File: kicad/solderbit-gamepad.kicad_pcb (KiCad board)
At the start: 2 copper layers, 114.5 x 45 mm, 28 parts, among them J1 Microbit, SW1 MST22D18G2 125, U1 74HC165

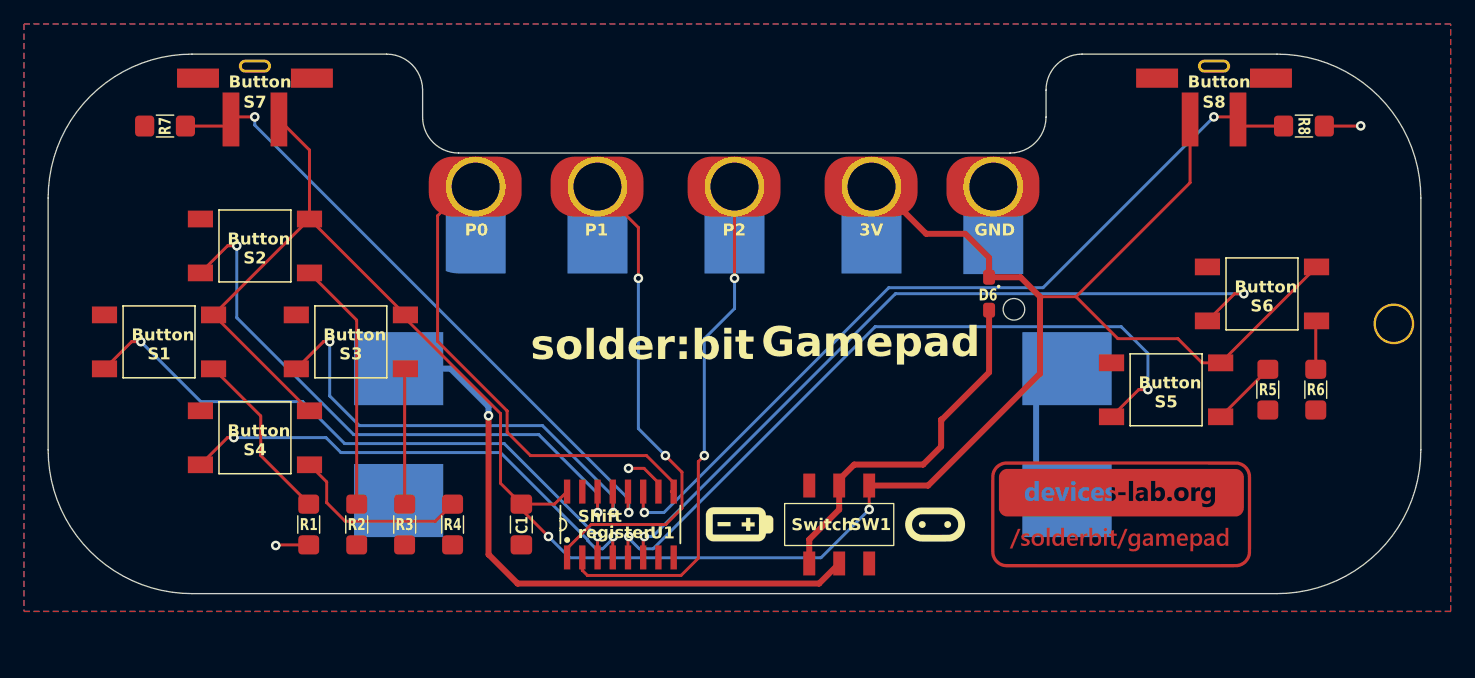
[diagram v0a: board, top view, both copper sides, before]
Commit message: Added all new project files and updated README.md for 2025 workshop
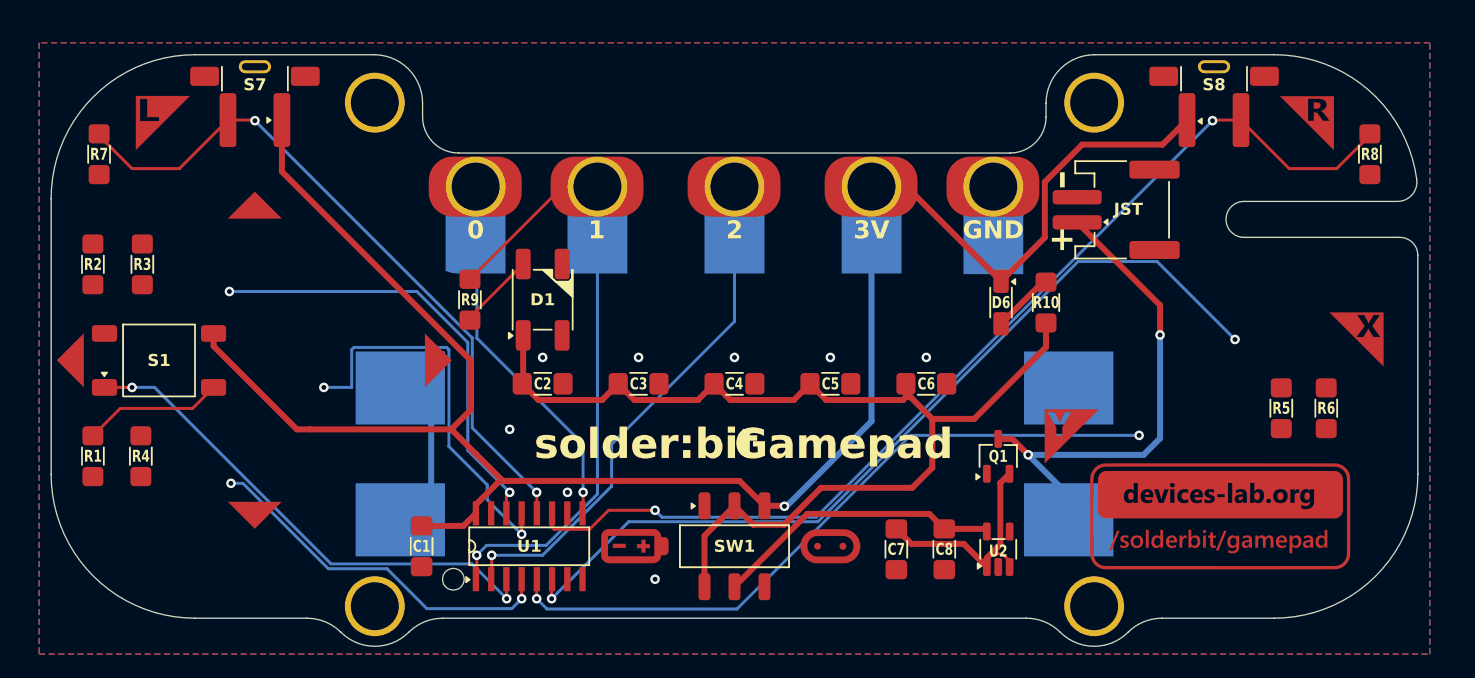
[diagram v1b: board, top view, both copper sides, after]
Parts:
- removed G2: ~, Solderbit_Gamepad:Pro2_Logo
- removed G3: ~, Solderbit_Gamepad:Key_Chain_Hole
- removed G5: ~, Solderbit_Gamepad:LSS_L
- removed G6: ~, Solderbit_Gamepad:LSS_R
- removed S2, S3, S4, S5, S6: TS-1002S-AR06026, Solderbit_Gamepad:Tactile_Switch
- added ?: , clipboard:40dc3674-e08b-4222-942d-4811059c9af4, B.Cu at (90.2, 67.1)
- added C2: 1uF, Solderbit_Gamepad:1206_Capacitor, F.Cu at (88.3, 64.0)
- added C3: 1uF, Solderbit_Gamepad:1206_Capacitor, F.Cu at (96.3, 64.0)
- added C4: 1uF, Solderbit_Gamepad:1206_Capacitor, F.Cu at (104.3, 64.0)
- added C5: 1uF, Solderbit_Gamepad:1206_Capacitor, F.Cu at (112.3, 64.0)
- added C6: 1uF, Solderbit_Gamepad:1206_Capacitor, F.Cu at (120.3, 64.0)
- added C7: 1uF, Solderbit_Gamepad:1206_Capacitor, F.Cu at (117.8, 77.8)
- added C8: 1uF, Solderbit_Gamepad:1206_Capacitor, F.Cu at (121.8, 77.8)
- added D1: WS2812B, Solderbit_Gamepad:NeoPixel_WS2812B, F.Cu at (88.3, 57.0)
- added H1: MountingHole_Pad, Solderbit_Gamepad:MountingHole_Pad, F.Cu at (74.3, 40.6)
- added H2: MountingHole_Pad, Solderbit_Gamepad:MountingHole_Pad, F.Cu at (134.3, 40.6)
- added H3: MountingHole_Pad, Solderbit_Gamepad:MountingHole_Pad, F.Cu at (74.3, 82.6)
- added H4: MountingHole_Pad, Solderbit_Gamepad:MountingHole_Pad, F.Cu at (134.3, 82.6)
- added J2: S2B-PH-SM4-TB(LF)(SN), Solderbit_Gamepad:JST_PH_S2B-PH-SM4-TB, F.Cu at (136.0, 49.5)
- added Q1: DMG2045U, Solderbit_Gamepad:TSOT-23, F.Cu at (126.3, 70.1)
- added R10: 3R, Solderbit_Gamepad:1206_Resistor, F.Cu at (130.2, 57.2)
- added R9: 300R, Solderbit_Gamepad:1206_Resistor, F.Cu at (82.2, 57.0)
- added Ref**: Val**, Solderbit_Gamepad:Button_Label_Y, F.Cu at (132.4, 68.4)
- added Ref**: Val**, Solderbit_Gamepad:Button_Label_Arrow, F.Cu at (47.8, 62.0)
- added Ref**: Val**, Solderbit_Gamepad:Button_Label_Arrow, F.Cu at (64.2, 48.0)
- added Ref**: Val**, Solderbit_Gamepad:Button_Label_Arrow, F.Cu at (80.7, 62.0)
- added Ref**: Val**, Solderbit_Gamepad:Button_Label_L, F.Cu at (56.5, 42.3)
- added Ref**: Val**, Solderbit_Gamepad:Button_Label_X, F.Cu at (156.2, 60.3)
- added Ref**: Val**, Solderbit_Gamepad:Button_Label_Arrow, F.Cu at (64.2, 76.1)
- added Ref**: Val**, Solderbit_Gamepad:Button_Label_R, F.Cu at (152.0, 42.3)
- added Ref**: Val**, Solderbit_Gamepad:Pro2_Logo, B.Cu at (62.2, 46.6)
- added U2: NCP114ASN330T1G, Solderbit_Gamepad:TSOP-5, F.Cu at (126.3, 77.8)
- BT1, G4: moved to B.Cu
- D6: value BAT60B -> MBR120VLSFT1G; footprint Solderbit_Gamepad:Schottky_Diode_SOD-323 -> Solderbit_Gamepad:SOD-123FL
- J1: value Microbit -> Microbit_Edge_Connector
- S1: value TS-1002S-AR06026 -> KH-6X6X6H-STM
- U1: value 74HC165 -> 74HC165D,653
- moved R2 30.9 mm to (50.8, 54.0)
- moved R3 30.8 mm to (54.9, 54.0)
- moved R4 26.6 mm to (54.8, 70.0)
- moved R1 18.9 mm to (50.8, 70.0)
- moved G4 10.2 mm to (62.3, 55.6), turned to 180 degrees
- moved SW1 8.92 mm to (104.3, 77.6)
- moved C1 8.52 mm to (78.2, 77.6)
- moved G1 8.27 mm to (144.8, 75.1)
- moved U1 7.81 mm to (87.2, 77.6)
- moved R7 5.98 mm to (51.3, 44.9), turned to 90 degrees
- moved R8 5.98 mm to (157.3, 44.9), turned to 90 degrees
- moved R5 1.92 mm to (149.9, 66.0)
- moved R6 1.78 mm to (153.6, 66.0)
- moved BT1 1.62 mm to (104.3, 69.9)
- moved S1 1.55 mm to (56.3, 62.1)
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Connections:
- D6 pad 2: Vneo -> Net-(D6-Pad2)
- R2 pad 1: Net-(R2-Pad1) -> unconnected-(R2-Pad1)
- R3 pad 1: Net-(R3-Pad1) -> unconnected-(R3-Pad1)
- R4 pad 1: Net-(R4-Pad1) -> unconnected-(R4-Pad1)
- R5 pad 1: Net-(R5-Pad1) -> unconnected-(R5-Pad1)
- R6 pad 1: Net-(R6-Pad1) -> unconnected-(R6-Pad1)
- SW1 pad 5: Net-(BT1-+) -> Net-(SW1B-B)
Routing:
- net Vneo: track 30.7 -> 89.5 mm
- net Vubit: track 192.6 -> 164.0 mm, vias 2 -> 1
- net Net-(SW1B-B): track 0.00 -> 24.2 mm
- net Net-(R2-Pad1): track 20.9 -> 0.00 mm
- net Net-(Q1-S): track 0.00 -> 19.8 mm
- net BTN_R_BUMP: track 69.1 -> 87.0 mm
- net Net-(R4-Pad1): track 15.5 -> 0.00 mm
- net BTN_UP: track 49.5 -> 37.5 mm
- net BTN_DOWN: track 42.0 -> 30.6 mm
- net Net-(R3-Pad1): track 11.3 -> 0.00 mm
- net SER: track 41.5 -> 30.9 mm, vias 0 -> 1
- net Net-(BT1-+): track 52.1 -> 42.3 mm, vias 1 -> 2
- net GND: track 9.54 -> 0.00 mm, vias 3 -> 8
- net PL/DATA: track 44.8 -> 53.7 mm, vias 2 -> 1
- net BTN_LEFT: track 51.3 -> 42.5 mm
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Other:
- board size 114.5 x 45 mm -> 114 x 49.3 mm
- board text added: "After completing the schamatic, you need to update the PCB. Go to {dblquote}Tools{dblquote} > {dblquote}Update PCB from Schematic...{dblquote} (or press F8). Follow the dialogue, and all components will appear in the corner with {dblquote}ratsnet{dblquote}. Reposition the compoenents, and route them according to the ratsnet."
- board text added: "H change layer view Alt+3 3D preview R rotate item Shift+M move item X add tracks B fill zones CTRL+B unfill zones"
- board text added: "Useful keyboard shortcuts"
- board text added: "Your task"
- board text added: "v0.7"
- board text removed: "v0.5"
